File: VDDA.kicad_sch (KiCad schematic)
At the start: 44 parts, among them J7 Conn_01x02, Q3 AO3401A, U8 L78M05ABDT-TR

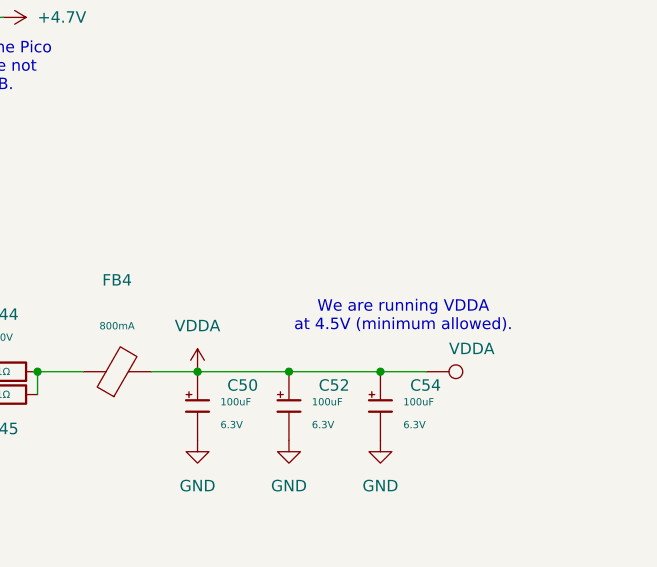
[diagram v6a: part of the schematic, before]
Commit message: Added test points
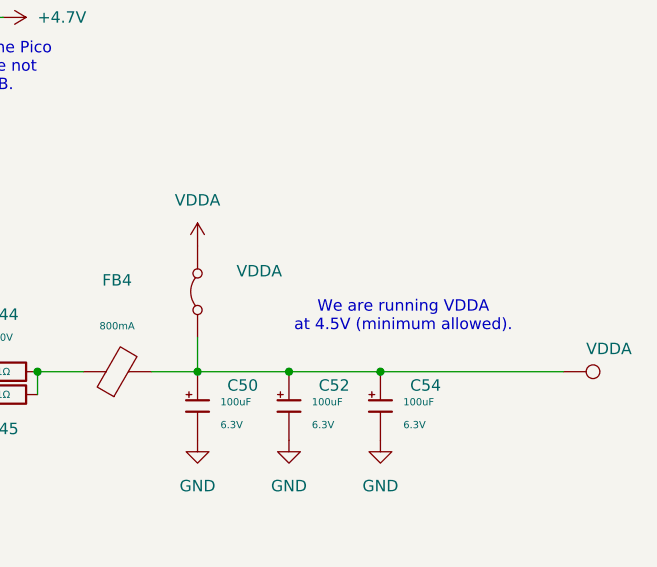
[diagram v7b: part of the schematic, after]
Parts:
- added JP7: VDDA, Jumper:SolderJumper-2_P1.3mm_Bridged2Bar_RoundedPad1.0x1.5mm, symbol Jumper:Jumper_2_Bridged
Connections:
- net VDDA: now also JP7.2 (B); no longer C50.1, C52.1, C54.1, FB4.2, TP5.1
- new net: C50.1, C52.1, C54.1, FB4.2, JP7.1 (A), TP5.1
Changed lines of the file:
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@@
 	)
 	(junction
-		(at 228.6 100.33)
-		(diameter 0)
-		(color 0 0 0 0)
-	)
-	(junction
 		(at 171.45 100.33)
 		(diameter 0)
@@
 	)
 	(junction
+		(at 228.6 100.33)
+		(diameter 0)
+		(color 0 0 0 0)
+	)
+	(junction
 		(at 119.38 100.33)
 		(diameter 0)
@@
 	(wire
 		(pts
-			(xy 228.6 100.33) (xy 233.68 100.33)
+			(xy 228.6 100.33) (xy 248.92 100.33)
 		)
 		(stroke
@@
 	(wire
 		(pts
+			(xy 208.28 96.52) (xy 208.28 100.33)
+		)
+		(stroke
+			(width 0)
+			(type default)
+		)
+	)
+	(wire
+		(pts
 			(xy 171.45 50.8) (xy 171.45 60.96)
 		)
@@
 	(symbol
 		(lib_id "Connector:TestPoint")
-		(at 233.68 100.33 270)
+		(at 248.92 100.33 270)
 		(unit 1)
 		(body_style 1)
@@
 		(dnp no)
 		(property "Reference" "TP5"
-			(at 240.03 100.33 90)
+			(at 255.27 100.33 90)
 			(hide yes)
 			(show_name no)
@@
 		)
 		(property "Value" "VDDA"
-			(at 236.22 97.79 90)
+			(at 251.46 97.79 90)
 			(show_name no)
 			(do_not_autoplace no)
@@
 		)
 		(property "Footprint" "TestPoint:TestPoint_THTPad_D2.5mm_Drill1.2mm"
-			(at 233.68 105.41 0)
+			(at 248.92 105.41 0)
 			(hide yes)
 			(show_name no)
@@
 		)
 		(property "Datasheet" ""
-			(at 233.68 105.41 0)
+			(at 248.92 105.41 0)
 			(hide yes)
 			(show_name no)
@@
 		)
 		(property "Description" ""
-			(at 233.68 100.33 0)
+			(at 248.92 100.33 0)
 			(hide yes)
 			(show_name no)
@@
 		)
 		(property "JLCPCB #" ""
-			(at 233.68 100.33 0)
+			(at 248.92 100.33 0)
 			(hide yes)
 			(show_name no)
@@
 	(symbol
 		(lib_id "power:VDDA")
-		(at 208.28 100.33 0)
+		(at 208.28 86.36 0)
 		(unit 1)
 		(body_style 1)
@@
 		(fields_autoplaced yes)
 		(property "Reference" "#PWR097"
-			(at 208.28 104.14 0)
+			(at 208.28 90.17 0)
 			(hide yes)
 			(show_name no)
@@
 		)
 		(property "Value" "VDDA"
-			(at 208.28 95.25 0)
+			(at 208.28 81.28 0)
 			(show_name no)
 			(do_not_autoplace no)
@@
 		)
 		(property "Footprint" ""
-			(at 208.28 100.33 0)
+			(at 208.28 86.36 0)
 			(hide yes)
 			(show_name no)
@@
 		)
 		(property "Datasheet" ""
-			(at 208.28 100.33 0)
+			(at 208.28 86.36 0)
 			(hide yes)
 			(show_name no)
@@
 		)
 		(property "Description" ""
-			(at 208.28 100.33 0)
+			(at 208.28 86.36 0)
 			(hide yes)
 			(show_name no)
@@
 					(unit 1)
 				)
+			)
+		)
+	)
+	(symbol
+		(lib_id "Jumper:Jumper_2_Bridged")
+		(at 208.28 91.44 90)
+		(unit 1)
+		(body_style 1)
+		(exclude_from_sim yes)
+		(in_bom yes)
+		(on_board yes)
+		(in_pos_files yes)
+		(dnp no)
+		(property "Reference" "JP7"
+			(at 205.74 91.44 0)
+			(hide yes)
+			(show_name no)
+			(do_not_autoplace no)
+			(effects
+				(font
+					(size 1.27 1.27)
+				)
+			)
+		)
+		(property "Value" "VDDA"
+			(at 215.138 89.154 90)
+			(show_name no)
+			(do_not_autoplace no)
+			(effects
+				(font
+					(size 1.27 1.27)
+				)
+			)
+		)
+		(property "Footprint" "Jumper:SolderJumper-2_P1.3mm_Bridged2Bar_RoundedPad1.0x1.5mm"
+			(at 208.28 91.44 0)
+			(hide yes)
+			(show_name no)
+			(do_not_autoplace no)
+			(effects
+				(font
+					(size 1.27 1.27)
+				)
+			)
+		)
+		(property "Datasheet" ""
+			(at 208.28 91.44 0)
+			(hide yes)
+			(show_name no)
+			(do_not_autoplace no)
+			(effects
+				(font
+					(size 1.27 1.27)
+				)
+			)
+		)
+		(property "Description" "Jumper, 2-pole, closed/bridged"
+			(at 208.28 91.44 0)
+			(hide yes)
+			(show_name no)
+			(do_not_autoplace no)
+			(effects
+				(font
+					(size 1.27 1.27)
+				)
+			)
+		)
+		(property "JLCPCB #" ""
+			(at 208.28 91.44 0)
+			(hide yes)
+			(show_name no)
+			(do_not_autoplace no)
+			(effects
+				(font
+					(size 1.27 1.27)
+				)
+			)
+		)
+		(pin "2"
+		)
+		(pin "1"
+		)
+		(instances
+			(project "DDC_SDR"
+				(path "/7dfef218-ca21-47b0-a8d3-67c7d55cb9d2/48946e56-e004-4035-9a82-30e09af92ded"
+					(reference "JP7")
+					(unit 1)
+				)

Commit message: Added Prototype Area
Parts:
- TP4, TP5, TP6: footprint TestPoint:TestPoint_THTPad_D2.5mm_Drill1.2mm -> RP2040_minimal:TestPoint_THTPad_D2.5mm_Drill1.2mm
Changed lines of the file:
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@@
 			)
 		)
-		(property "Footprint" "TestPoint:TestPoint_THTPad_D2.5mm_Drill1.2mm"
+		(property "Footprint" "RP2040_minimal:TestPoint_THTPad_D2.5mm_Drill1.2mm"
 			(at 233.68 140.97 0)
 			(hide yes)
@@
 			)
 		)
-		(property "Footprint" "TestPoint:TestPoint_THTPad_D2.5mm_Drill1.2mm"
+		(property "Footprint" "RP2040_minimal:TestPoint_THTPad_D2.5mm_Drill1.2mm"
 			(at 248.92 105.41 0)
 			(hide yes)
@@
 			)
 		)
-		(property "Footprint" "TestPoint:TestPoint_THTPad_D2.5mm_Drill1.2mm"
+		(property "Footprint" "RP2040_minimal:TestPoint_THTPad_D2.5mm_Drill1.2mm"
 			(at 62.23 95.25 0)
 			(hide yes)
